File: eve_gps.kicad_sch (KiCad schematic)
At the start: 10 parts, among them J5 BMI-S-101, J6 GNSS SMA

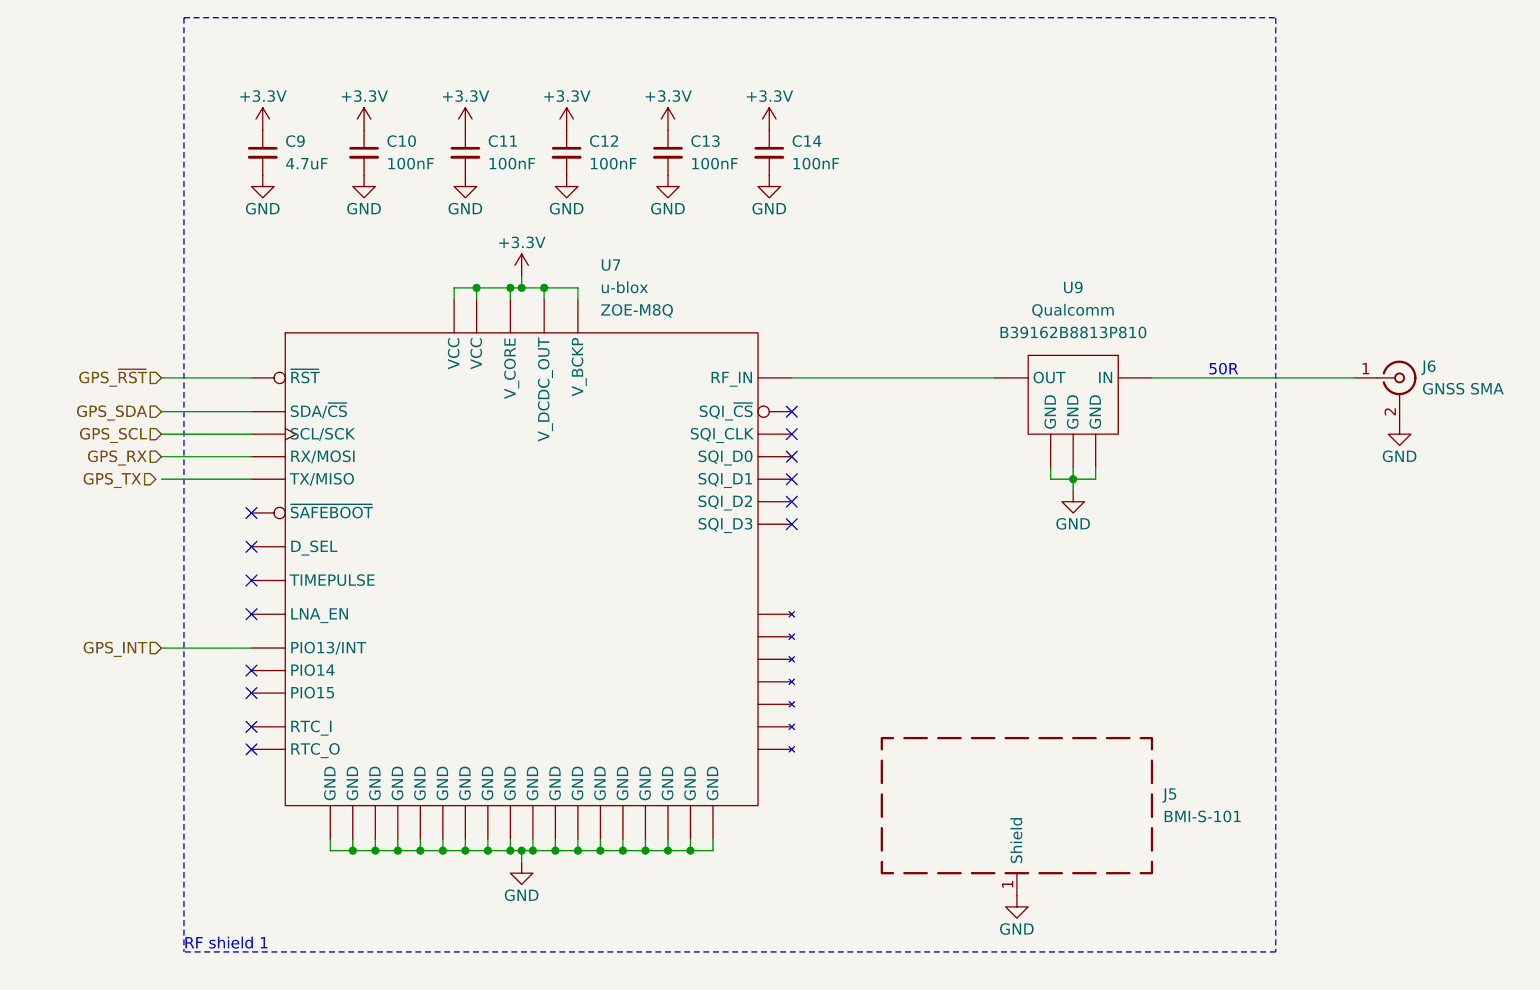
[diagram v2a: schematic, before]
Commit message: 8.02 Update; Also changed VRMs and added some notes
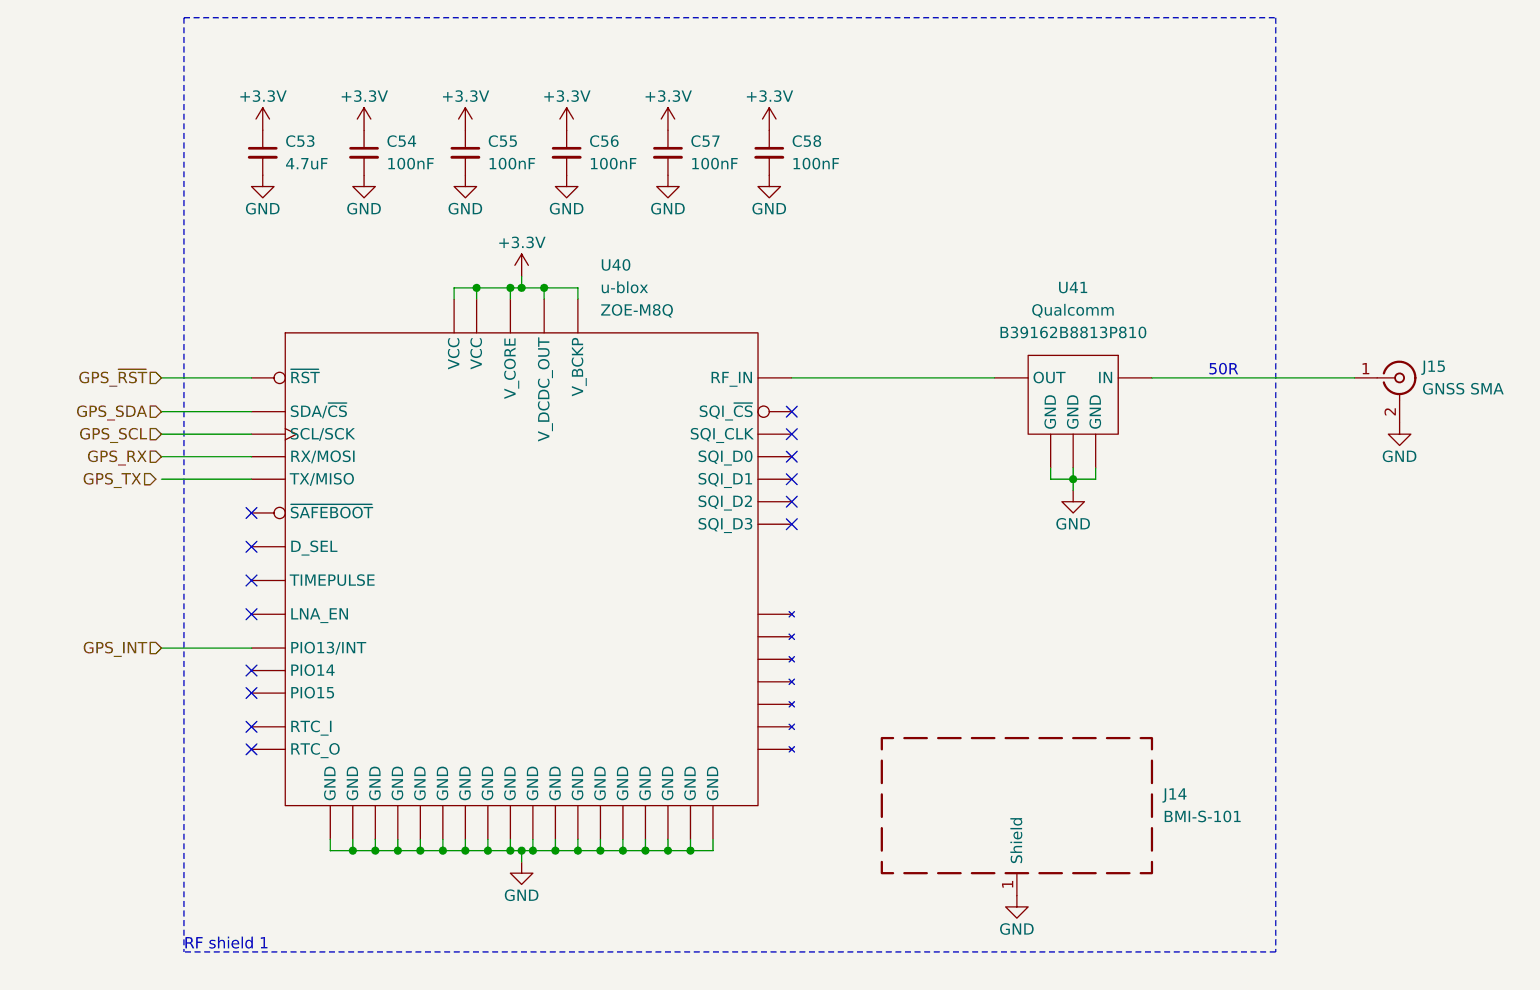
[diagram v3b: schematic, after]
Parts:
- renumbered C9 to C53, C10 to C54, C11 to C55, C12 to C56, C13 to C57, C14 to C58, J5 to J14, J6 to J15, U7 to U40, U9 to U41
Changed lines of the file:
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@@
 		(on_board yes)
 		(dnp no)
-		(property "Reference" "J6"
+		(property "Reference" "J15"
 			(at 222.25 83.185 0)
 			(effects
@@
 			(project "rocket2-ecu"
 				(path "/02606b2c-b376-4ffb-9781-f9cea3f70994/33703977-e0e9-46ee-bac6-f4661129caa1"
-					(reference "J6")
+					(reference "J15")
 					(unit 1)
 				)
@@
 		(on_board yes)
 		(dnp no)
-		(property "Reference" "C14"
+		(property "Reference" "C58"
 			(at 151.13 57.785 0)
 			(effects
@@
 			(project "rocket2-ecu"
 				(path "/02606b2c-b376-4ffb-9781-f9cea3f70994/33703977-e0e9-46ee-bac6-f4661129caa1"
-					(reference "C14")
+					(reference "C58")
 					(unit 1)
 				)
@@
 		(on_board yes)
 		(dnp no)
-		(property "Reference" "#PWR075"
+		(property "Reference" "#PWR0196"
 			(at 219.71 95.885 0)
 			(effects
@@
 			(project "rocket2-ecu"
 				(path "/02606b2c-b376-4ffb-9781-f9cea3f70994/33703977-e0e9-46ee-bac6-f4661129caa1"
-					(reference "#PWR075")
+					(reference "#PWR0196")
 					(unit 1)
 				)
@@
 		(on_board yes)
 		(dnp no)
-		(property "Reference" "#PWR058"
+		(property "Reference" "#PWR0186"
 			(at 120.65 76.835 0)
 			(effects
@@
 			(project "rocket2-ecu"
 				(path "/02606b2c-b376-4ffb-9781-f9cea3f70994/33703977-e0e9-46ee-bac6-f4661129caa1"
-					(reference "#PWR058")
+					(reference "#PWR0186")
 					(unit 1)
 				)
@@
 		(on_board yes)
 		(dnp no)
-		(property "Reference" "#PWR054"
+		(property "Reference" "#PWR0184"
 			(at 114.3 60.325 0)
 			(effects
@@
 			(project "rocket2-ecu"
 				(path "/02606b2c-b376-4ffb-9781-f9cea3f70994/33703977-e0e9-46ee-bac6-f4661129caa1"
-					(reference "#PWR054")
+					(reference "#PWR0184")
 					(unit 1)
 				)
@@
 		(on_board yes)
 		(dnp no)
-		(property "Reference" "#PWR067"
+		(property "Reference" "#PWR0193"
 			(at 148.59 67.945 0)
 			(effects
@@
 			(project "rocket2-ecu"
 				(path "/02606b2c-b376-4ffb-9781-f9cea3f70994/33703977-e0e9-46ee-bac6-f4661129caa1"
-					(reference "#PWR067")
+					(reference "#PWR0193")
 					(unit 1)
 				)
@@
 		(on_board yes)
 		(dnp no)
-		(property "Reference" "C9"
+		(property "Reference" "C53"
 			(at 93.98 57.785 0)
 			(effects
@@
 			(project "rocket2-ecu"
 				(path "/02606b2c-b376-4ffb-9781-f9cea3f70994/33703977-e0e9-46ee-bac6-f4661129caa1"
-					(reference "C9")
+					(reference "C53")
 					(unit 1)
 				)
@@
 		(on_board yes)
 		(dnp no)
-		(property "Reference" "C11"
+		(property "Reference" "C55"
 			(at 116.84 57.785 0)
 			(effects
@@
 			(project "rocket2-ecu"
 				(path "/02606b2c-b376-4ffb-9781-f9cea3f70994/33703977-e0e9-46ee-bac6-f4661129caa1"
-					(reference "C11")
+					(reference "C55")
 					(unit 1)
 				)
@@
 		(on_board yes)
 		(dnp no)
-		(property "Reference" "#PWR072"
+		(property "Reference" "#PWR0195"
 			(at 182.88 103.505 0)
 			(effects
@@
 			(project "rocket2-ecu"
 				(path "/02606b2c-b376-4ffb-9781-f9cea3f70994/33703977-e0e9-46ee-bac6-f4661129caa1"
-					(reference "#PWR072")
+					(reference "#PWR0195")
 					(unit 1)
 				)
@@
 		(on_board yes)
 		(dnp no)
-		(property "Reference" "#PWR051"
+		(property "Reference" "#PWR0181"
 			(at 91.44 67.945 0)
 			(effects
@@
 			(project "rocket2-ecu"
 				(path "/02606b2c-b376-4ffb-9781-f9cea3f70994/33703977-e0e9-46ee-bac6-f4661129caa1"
-					(reference "#PWR051")
+					(reference "#PWR0181")
 					(unit 1)
 				)
@@
 		(on_board yes)
 		(dnp no)
-		(property "Reference" "C10"
+		(property "Reference" "C54"
 			(at 105.41 57.785 0)
 			(effects
@@
 			(project "rocket2-ecu"
 				(path "/02606b2c-b376-4ffb-9781-f9cea3f70994/33703977-e0e9-46ee-bac6-f4661129caa1"
-					(reference "C10")
+					(reference "C54")
 					(unit 1)
 				)
@@
 		(on_board yes)
 		(dnp no)
-		(property "Reference" "C13"
+		(property "Reference" "C57"
 			(at 139.7 57.785 0)
 			(effects
@@
 			(project "rocket2-ecu"
 				(path "/02606b2c-b376-4ffb-9781-f9cea3f70994/33703977-e0e9-46ee-bac6-f4661129caa1"
-					(reference "C13")
+					(reference "C57")
 					(unit 1)
 				)
@@
 		(on_board yes)
 		(dnp no)
-		(property "Reference" "#PWR060"
+		(property "Reference" "#PWR0188"
 			(at 125.73 60.325 0)
 			(effects
@@
 			(project "rocket2-ecu"
 				(path "/02606b2c-b376-4ffb-9781-f9cea3f70994/33703977-e0e9-46ee-bac6-f4661129caa1"
-					(reference "#PWR060")
+					(reference "#PWR0188")
 					(unit 1)
 				)
@@
 		(on_board yes)
 		(dnp no)
-		(property "Reference" "#PWR065"
+		(property "Reference" "#PWR0191"
 			(at 137.16 67.945 0)
 			(effects
@@
 			(project "rocket2-ecu"
 				(path "/02606b2c-b376-4ffb-9781-f9cea3f70994/33703977-e0e9-46ee-bac6-f4661129caa1"
-					(reference "#PWR065")
+					(reference "#PWR0191")
 					(unit 1)
 				)
@@
 		(on_board yes)
 		(dnp no)
-		(property "Reference" "#PWR052"
+		(property "Reference" "#PWR0182"
 			(at 102.87 60.325 0)
 			(effects
@@
 			(project "rocket2-ecu"
 				(path "/02606b2c-b376-4ffb-9781-f9cea3f70994/33703977-e0e9-46ee-bac6-f4661129caa1"
-					(reference "#PWR052")
+					(reference "#PWR0182")
 					(unit 1)
 				)
@@
 		(on_board yes)
 		(dnp no)
-		(property "Reference" "#PWR055"
+		(property "Reference" "#PWR0185"
 			(at 114.3 67.945 0)
 			(effects
@@
 			(project "rocket2-ecu"
 				(path "/02606b2c-b376-4ffb-9781-f9cea3f70994/33703977-e0e9-46ee-bac6-f4661129caa1"
-					(reference "#PWR055")
+					(reference "#PWR0185")
 					(unit 1)
 				)
@@
 		(on_board yes)
 		(dnp no)
-		(property "Reference" "#PWR066"
+		(property "Reference" "#PWR0192"
 			(at 148.59 60.325 0)
 			(effects
@@
 			(project "rocket2-ecu"
 				(path "/02606b2c-b376-4ffb-9781-f9cea3f70994/33703977-e0e9-46ee-bac6-f4661129caa1"
-					(reference "#PWR066")
+					(reference "#PWR0192")
 					(unit 1)
 				)
@@
 		(on_board yes)
 		(dnp no)
-		(property "Reference" "#PWR070"
+		(property "Reference" "#PWR0194"
 			(at 176.53 149.225 0)
 			(effects
@@
 			(project "rocket2-ecu"
 				(path "/02606b2c-b376-4ffb-9781-f9cea3f70994/33703977-e0e9-46ee-bac6-f4661129caa1"
-					(reference "#PWR070")
+					(reference "#PWR0194")
 					(unit 1)
 				)
@@
 		(dnp no)
 		(fields_autoplaced yes)
-		(property "Reference" "J5"
+		(property "Reference" "J14"
 			(at 193.04 131.445 0)
 			(effects
@@
 			(project "rocket2-ecu"
 				(path "/02606b2c-b376-4ffb-9781-f9cea3f70994/33703977-e0e9-46ee-bac6-f4661129caa1"
-					(reference "J5")
+					(reference "J14")
 					(unit 1)
 				)
@@
 		(on_board yes)
 		(dnp no)
-		(property "Reference" "C12"
+		(property "Reference" "C56"
 			(at 128.27 57.785 0)
 			(effects
@@
 			(project "rocket2-ecu"
 				(path "/02606b2c-b376-4ffb-9781-f9cea3f70994/33703977-e0e9-46ee-bac6-f4661129caa1"
-					(reference "C12")
+					(reference "C56")
 					(unit 1)
 				)
@@
 		(on_board yes)
 		(dnp no)
-		(property "Reference" "#PWR059"
+		(property "Reference" "#PWR0187"
 			(at 120.65 145.415 0)
 			(effects
@@
 			(project "rocket2-ecu"
 				(path "/02606b2c-b376-4ffb-9781-f9cea3f70994/33703977-e0e9-46ee-bac6-f4661129caa1"
-					(reference "#PWR059")
+					(reference "#PWR0187")
 					(unit 1)
 				)
@@
 		(on_board yes)
 		(dnp no)
-		(property "Reference" "#PWR061"
+		(property "Reference" "#PWR0189"
 			(at 125.73 67.945 0)
 			(effects
@@
 			(project "rocket2-ecu"
 				(path "/02606b2c-b376-4ffb-9781-f9cea3f70994/33703977-e0e9-46ee-bac6-f4661129caa1"
-					(reference "#PWR061")
+					(reference "#PWR0189")
 					(unit 1)
 				)
@@
 		(dnp no)
 		(fields_autoplaced yes)
-		(property "Reference" "U9"
+		(property "Reference" "U41"
 			(at 182.88 74.295 0)
 			(effects
@@
 			(project "rocket2-ecu"
 				(path "/02606b2c-b376-4ffb-9781-f9cea3f70994/33703977-e0e9-46ee-bac6-f4661129caa1"
-					(reference "U9")
+					(reference "U41")
 					(unit 1)
 				)
@@
 		(on_board yes)
 		(dnp no)
-		(property "Reference" "#PWR050"
+		(property "Reference" "#PWR0180"
 			(at 91.44 60.325 0)
 			(effects
@@
 			(project "rocket2-ecu"
 				(path "/02606b2c-b376-4ffb-9781-f9cea3f70994/33703977-e0e9-46ee-bac6-f4661129caa1"
-					(reference "#PWR050")
+					(reference "#PWR0180")
 					(unit 1)
 				)
@@
 		(on_board yes)
 		(dnp no)
-		(property "Reference" "#PWR053"
+		(property "Reference" "#PWR0183"
 			(at 102.87 67.945 0)
 			(effects
@@
 			(project "rocket2-ecu"
 				(path "/02606b2c-b376-4ffb-9781-f9cea3f70994/33703977-e0e9-46ee-bac6-f4661129caa1"
-					(reference "#PWR053")
+					(reference "#PWR0183")
 					(unit 1)
 				)
@@
 		(on_board yes)
 		(dnp no)
-		(property "Reference" "U7"
+		(property "Reference" "U40"
 			(at 129.54 71.755 0)
 			(effects
@@
 			(project "rocket2-ecu"
 				(path "/02606b2c-b376-4ffb-9781-f9cea3f70994/33703977-e0e9-46ee-bac6-f4661129caa1"
-					(reference "U7")
+					(reference "U40")
 					(unit 1)
 				)
@@
 		(on_board yes)
 		(dnp no)
-		(property "Reference" "#PWR064"
+		(property "Reference" "#PWR0190"
 			(at 137.16 60.325 0)
 			(effects
@@
 			(project "rocket2-ecu"
 				(path "/02606b2c-b376-4ffb-9781-f9cea3f70994/33703977-e0e9-46ee-bac6-f4661129caa1"
-					(reference "#PWR064")
-					(unit 1)
-				)
+					(reference "#PWR0190")
+					(unit 1)
+				)

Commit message: ECU essentially reviewable
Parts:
- removed U41: ~, EVE:B39162B8813P810, symbol EVE:B39162B8813P810
- renumbered U40 to U39
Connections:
- net at J15.1 (In): now also U39.A4 (RF_IN)
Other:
- moved on the sheet: C53, C54, C55, C56, C57, C58, J14, J15, U39

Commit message: addressed PR comments
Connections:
- net GPS_TX: now also U39.J5 (TX/MISO)
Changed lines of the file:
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@@
 	(hierarchical_label "GPS_TX"
 		(shape input)
-		(at 78.105 97.79 180)
+		(at 78.74 97.79 180)
 		(fields_autoplaced yes)
 		(effects
@@
 		(on_board yes)
 		(dnp no)
-		(property "Reference" "#PWR0193"
+		(property "Reference" "#PWR0194"
 			(at 194.31 97.79 0)
 			(effects
@@
 			(project "rocket2-ecu"
 				(path "/02606b2c-b376-4ffb-9781-f9cea3f70994/33703977-e0e9-46ee-bac6-f4661129caa1"
-					(reference "#PWR0193")
+					(reference "#PWR0194")
 					(unit 1)
 				)
@@
 		(on_board yes)
 		(dnp no)
-		(property "Reference" "#PWR0184"
+		(property "Reference" "#PWR0185"
 			(at 119.38 78.74 0)
 			(effects
@@
 			(project "rocket2-ecu"
 				(path "/02606b2c-b376-4ffb-9781-f9cea3f70994/33703977-e0e9-46ee-bac6-f4661129caa1"
-					(reference "#PWR0184")
+					(reference "#PWR0185")
 					(unit 1)
 				)
@@
 		(on_board yes)
 		(dnp no)
-		(property "Reference" "#PWR0182"
+		(property "Reference" "#PWR0183"
 			(at 113.03 62.23 0)
 			(effects
@@
 			(project "rocket2-ecu"
 				(path "/02606b2c-b376-4ffb-9781-f9cea3f70994/33703977-e0e9-46ee-bac6-f4661129caa1"
-					(reference "#PWR0182")
+					(reference "#PWR0183")
 					(unit 1)
 				)
@@
 		(on_board yes)
 		(dnp no)
-		(property "Reference" "#PWR0191"
+		(property "Reference" "#PWR0192"
 			(at 147.32 69.85 0)
 			(effects
@@
 			(project "rocket2-ecu"
 				(path "/02606b2c-b376-4ffb-9781-f9cea3f70994/33703977-e0e9-46ee-bac6-f4661129caa1"
-					(reference "#PWR0191")
+					(reference "#PWR0192")
 					(unit 1)
 				)
@@
 		(on_board yes)
 		(dnp no)
-		(property "Reference" "#PWR0179"
+		(property "Reference" "#PWR0180"
 			(at 90.17 69.85 0)
 			(effects
@@
 			(project "rocket2-ecu"
 				(path "/02606b2c-b376-4ffb-9781-f9cea3f70994/33703977-e0e9-46ee-bac6-f4661129caa1"
-					(reference "#PWR0179")
+					(reference "#PWR0180")
 					(unit 1)
 				)
@@
 		(on_board yes)
 		(dnp no)
-		(property "Reference" "#PWR0186"
+		(property "Reference" "#PWR0187"
 			(at 124.46 62.23 0)
 			(effects
@@
 			(project "rocket2-ecu"
 				(path "/02606b2c-b376-4ffb-9781-f9cea3f70994/33703977-e0e9-46ee-bac6-f4661129caa1"
-					(reference "#PWR0186")
+					(reference "#PWR0187")
 					(unit 1)
 				)
@@
 		(on_board yes)
 		(dnp no)
-		(property "Reference" "#PWR0189"
+		(property "Reference" "#PWR0190"
 			(at 135.89 69.85 0)
 			(effects
@@
 			(project "rocket2-ecu"
 				(path "/02606b2c-b376-4ffb-9781-f9cea3f70994/33703977-e0e9-46ee-bac6-f4661129caa1"
-					(reference "#PWR0189")
+					(reference "#PWR0190")
 					(unit 1)
 				)
@@
 		(on_board yes)
 		(dnp no)
-		(property "Reference" "#PWR0180"
+		(property "Reference" "#PWR0181"
 			(at 101.6 62.23 0)
 			(effects
@@
 			(project "rocket2-ecu"
 				(path "/02606b2c-b376-4ffb-9781-f9cea3f70994/33703977-e0e9-46ee-bac6-f4661129caa1"
-					(reference "#PWR0180")
+					(reference "#PWR0181")
 					(unit 1)
 				)
@@
 		(on_board yes)
 		(dnp no)
-		(property "Reference" "#PWR0183"
+		(property "Reference" "#PWR0184"
 			(at 113.03 69.85 0)
 			(effects
@@
 			(project "rocket2-ecu"
 				(path "/02606b2c-b376-4ffb-9781-f9cea3f70994/33703977-e0e9-46ee-bac6-f4661129caa1"
-					(reference "#PWR0183")
+					(reference "#PWR0184")
 					(unit 1)
 				)
@@
 		(on_board yes)
 		(dnp no)
-		(property "Reference" "#PWR0190"
+		(property "Reference" "#PWR0191"
 			(at 147.32 62.23 0)
 			(effects
@@
 			(project "rocket2-ecu"
 				(path "/02606b2c-b376-4ffb-9781-f9cea3f70994/33703977-e0e9-46ee-bac6-f4661129caa1"
-					(reference "#PWR0190")
+					(reference "#PWR0191")
 					(unit 1)
 				)
@@
 		(on_board yes)
 		(dnp no)
-		(property "Reference" "#PWR0192"
+		(property "Reference" "#PWR0193"
 			(at 168.91 151.13 0)
 			(effects
@@
 			(project "rocket2-ecu"
 				(path "/02606b2c-b376-4ffb-9781-f9cea3f70994/33703977-e0e9-46ee-bac6-f4661129caa1"
-					(reference "#PWR0192")
+					(reference "#PWR0193")
 					(unit 1)
 				)
@@
 		(on_board yes)
 		(dnp no)
-		(property "Reference" "#PWR0185"
+		(property "Reference" "#PWR0186"
 			(at 119.38 147.32 0)
 			(effects
@@
 			(project "rocket2-ecu"
 				(path "/02606b2c-b376-4ffb-9781-f9cea3f70994/33703977-e0e9-46ee-bac6-f4661129caa1"
-					(reference "#PWR0185")
+					(reference "#PWR0186")
 					(unit 1)
 				)
@@
 		(on_board yes)
 		(dnp no)
-		(property "Reference" "#PWR0187"
+		(property "Reference" "#PWR0188"
 			(at 124.46 69.85 0)
 			(effects
@@
 			(project "rocket2-ecu"
 				(path "/02606b2c-b376-4ffb-9781-f9cea3f70994/33703977-e0e9-46ee-bac6-f4661129caa1"
-					(reference "#PWR0187")
+					(reference "#PWR0188")
 					(unit 1)
 				)
@@
 		(on_board yes)
 		(dnp no)
-		(property "Reference" "#PWR0178"
+		(property "Reference" "#PWR0179"
 			(at 90.17 62.23 0)
 			(effects
@@
 			(project "rocket2-ecu"
 				(path "/02606b2c-b376-4ffb-9781-f9cea3f70994/33703977-e0e9-46ee-bac6-f4661129caa1"
-					(reference "#PWR0178")
+					(reference "#PWR0179")
 					(unit 1)
 				)
@@
 		(on_board yes)
 		(dnp no)
-		(property "Reference" "#PWR0181"
+		(property "Reference" "#PWR0182"
 			(at 101.6 69.85 0)
 			(effects
@@
 			(project "rocket2-ecu"
 				(path "/02606b2c-b376-4ffb-9781-f9cea3f70994/33703977-e0e9-46ee-bac6-f4661129caa1"
-					(reference "#PWR0181")
+					(reference "#PWR0182")
 					(unit 1)
 				)
@@
 		(on_board yes)
 		(dnp no)
-		(property "Reference" "#PWR0188"
+		(property "Reference" "#PWR0189"
 			(at 135.89 62.23 0)
 			(effects
@@
 			(project "rocket2-ecu"
 				(path "/02606b2c-b376-4ffb-9781-f9cea3f70994/33703977-e0e9-46ee-bac6-f4661129caa1"
-					(reference "#PWR0188")
-					(unit 1)
-				)
+					(reference "#PWR0189")
+					(unit 1)
+				)

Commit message: Assigned almost all footprints
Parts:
- C53: Part # Generic 4.7uF 6.3V 0402 X7R MLCC -> Generic 0603 4.7uF 6.3V X7R MLCC
- C54, C55, C56, C57, C58: Part # Generic 100nF 6.3V 0402 X7R MLCC -> Generic 100nF 6.3V X7R 0402 MLCC
- U39: footprint UCIRP-KiCAD-Lib:ZOE-M8Q -> 0UCIRP-KiCAD-Lib:ZOE-M8Q
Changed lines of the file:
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@@
 			)
 		)
-		(property "Part #" "Generic 100nF 6.3V 0402 X7R MLCC"
+		(property "Part #" "Generic 100nF 6.3V X7R 0402 MLCC"
 			(at 147.32 60.96 0)
 			(effects
@@
 			)
 		)
-		(property "Part #" "Generic 4.7uF 6.3V 0402 X7R MLCC"
+		(property "Part #" "Generic 0603 4.7uF 6.3V X7R MLCC"
 			(at 90.17 60.96 0)
 			(effects
@@
 			)
 		)
-		(property "Part #" "Generic 100nF 6.3V 0402 X7R MLCC"
+		(property "Part #" "Generic 100nF 6.3V X7R 0402 MLCC"
 			(at 113.03 60.96 0)
 			(effects
@@
 			)
 		)
-		(property "Part #" "Generic 100nF 6.3V 0402 X7R MLCC"
+		(property "Part #" "Generic 100nF 6.3V X7R 0402 MLCC"
 			(at 101.6 60.96 0)
 			(effects
@@
 			)
 		)
-		(property "Part #" "Generic 100nF 6.3V 0402 X7R MLCC"
+		(property "Part #" "Generic 100nF 6.3V X7R 0402 MLCC"
 			(at 135.89 60.96 0)
 			(effects
@@
 			)
 		)
-		(property "Part #" "Generic 100nF 6.3V 0402 X7R MLCC"
+		(property "Part #" "Generic 100nF 6.3V X7R 0402 MLCC"
 			(at 124.46 60.96 0)
 			(effects
@@
 			)
 		)
-		(property "Footprint" "UCIRP-KiCAD-Lib:ZOE-M8Q"
+		(property "Footprint" "0UCIRP-KiCAD-Lib:ZOE-M8Q"
 			(at 119.38 107.95 0)
 			(effects
